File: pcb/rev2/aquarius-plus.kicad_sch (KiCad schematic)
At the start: 216 parts, among them J1 Cassette in, J10 Audio out, J11 Hand controller 2, J12 ESP USB Host, J13 Power in, J14 FPGA spare, J15 Expansion port, J16 ESP32 spare, J2 Cassette out, J3 Amphenol GSD090012SEU, J4 Printer, J5 Hand controller 1, J6 VGA, J7 DBG, J8 USB_A, J9 USB_A, Q1 BC847C, Q2 BC847C, SW1 SW_DPDT_x2, U1 XC3S200-4TQG144, U10 IS61C5128AS-25QLI, U11 74LVC4245APW, U12 74HC166, U13 SST39SF020A-55-4C-WHE, U14 74LVC4245APW, U15 LDL1117S33R, U16 MCP1700T-2502E/TT, U17 LD1117S12, U2 SN74CBTD3861PWR, U3 MAX3221ECPWR, U4 SN74CBTD3861PWR, U5 ESP32-S2-SOLO-N4R2, U6 SN74CBTD3861PWR, U7 Z84C0010AEG, U8 SN74CBTD3861PWR, U9 74HC166, X1 ECS-5032MV-143-CN-TR, X2 ECS-5032MV-480-BN-TR

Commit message: Working on rev2 PCB.
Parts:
- removed C47, C53: 100uF, Capacitor_SMD:CP_Elec_6.3x7.7, symbol Device:C_Polarized_Small
- removed C52, C56, C57, C58, C59, C60: 100nF, Capacitor_SMD:C_0603_1608Metric, symbol Device:C_Small
- removed C63, C66: 4.7uF, Capacitor_SMD:C_0603_1608Metric, symbol Device:C_Small
- removed J8, J9: USB_A, Connector_USB:USB_A_Molex_67643_Horizontal, symbol Connector:USB_A
- removed R10: DNP, Resistor_SMD:R_0603_1608Metric, symbol Device:R
- removed R100: 1, Resistor_SMD:R_0603_1608Metric, symbol Device:R
- removed R11, R2, R5, R6, R63, R64, R65, R66, R67, R68, R69, R70, R8, R91, R92, R93, R94, R95, R96, R97, R98: 4.7k, Resistor_SMD:R_0603_1608Metric, symbol Device:R
- removed R3, R4, R9: 220, Resistor_SMD:R_0603_1608Metric, symbol Device:R
- removed R7: 1k, Resistor_SMD:R_0603_1608Metric, symbol Device:R
- removed R73, R74, R75, R76: 33, Resistor_SMD:R_0603_1608Metric, symbol Device:R
- removed R77, R78, R79, R80: 15k, Resistor_SMD:R_0603_1608Metric, symbol Device:R
- removed U1: XC3S200-4TQG144, Package_QFP:TQFP-144_20x20mm_P0.5mm, symbol aquarius-plus:XC3S200-4TQG144
- removed U11, U14: 74LVC4245APW, Package_SO:TSSOP-24_4.4x7.8mm_P0.65mm, symbol Logic_LevelTranslator:SN74AVC8T245PW
- removed U12, U9: 74HC166, Package_SO:SOIC-16_3.9x9.9mm_P1.27mm, symbol 74xx:74LS166
- removed U13: SST39SF020A-55-4C-WHE, Package_SO:TSOP-I-32_12.4x8mm_P0.5mm, symbol aquarius-plus:SST39SF020A-55-4C-WHE
- removed U16: MCP1700T-2502E/TT, Package_TO_SOT_SMD:SOT-23, symbol Regulator_Linear:MCP1700-2502E_SOT23
- removed U2, U4, U6, U8: SN74CBTD3861PWR, Package_SO:TSSOP-24_4.4x7.8mm_P0.65mm, symbol 74xx:74CBTLV3861
- removed U5: ESP32-S2-SOLO-N4R2, aquarius-plus:ESP32-S2-SOLO-N4R2, symbol aquarius-plus:ESP32-S2-SOLO-N4R2
- removed X2: ECS-5032MV-480-BN-TR, Oscillator:Oscillator_SMD_SeikoEpson_SG8002LB-4Pin_5.0x3.2mm, symbol Oscillator:SG-5032CAN
- added C47: 100nF, Capacitor_SMD:C_0603_1608Metric, symbol Device:C_Small
- added Q3: 2N7002, Package_TO_SOT_SMD:SOT-23, symbol Transistor_FET:2N7002
- added R53: 220, Resistor_SMD:R_0603_1608Metric, symbol Device:R
- added U1: XC6SLX9-2TQG144C, Package_QFP:TQFP-144_20x20mm_P0.5mm, symbol aquarius-plus:XC6SLX9-2TQG144C
- added U11, U2, U4, U6: SN74CB3T3245PWR, Package_SO:TSSOP-20_4.4x6.5mm_P0.65mm, symbol aquarius-plus:SN74CB3T3245PWR
- added U5: ESP32-S3-WROOM-1-N4R2, aquarius-plus:ESP32-S2-SOLO-N4R2, symbol aquarius-plus:ESP32-S3-WROOM-1-N4R2
- added U8, U9: SN74AHCT1G125DBVR, Package_TO_SOT_SMD:SOT-23-5, symbol 74xGxx:74AHCT1G125
- J3: value Amphenol GSD090012SEU -> TF-03A; footprint Connector_Card:SD_TE_2041021 -> aquarius-plus:TF-03A
- R1: value 4.7k -> 10k
- X1: value ECS-5032MV-143-CN-TR -> SX3M14.31818M20F30TNN; footprint Oscillator:Oscillator_SMD_SeikoEpson_SG8002LB-4Pin_5.0x3.2mm -> Oscillator:Oscillator_SMD_SeikoEpson_SG8002CE-4Pin_3.2x2.5mm
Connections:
- net +2V5 is gone; now on net +3V3: C12.1, C17.1, C2.1, C22.1, C26.1, C7.1, R1.2
- net DE0 is gone; now on net D0: J15.26 (Pin_26)
- net DE1 is gone; now on net D1: J15.27 (Pin_27)
- net DE2 is gone; now on net D2: J15.28 (Pin_28)
- net DE3 is gone; now on net D3: J15.29 (Pin_29)
- net DE4 is gone; now on net D4: J15.30 (Pin_30)
- net DE5 is gone; now on net D5: J15.31 (Pin_31)
- net DE6 is gone; now on net D6: J15.32 (Pin_32)
- net DE7 is gone; now on net D7: J15.33 (Pin_33)
- net +1V2: now also C30.1, U1.128 (VCCINT), U1.19 (VCCINT), U1.28 (VCCINT), U1.52 (VCCINT), U1.89 (VCCINT)
- net +3V3: now also C35.1, C42.1, C43.1, C47.1, U1.103 (VCCO_1), U1.122 (VCCO_0), U1.125 (VCCO_0), U1.129 (VCCAUX), U1.135 (VCCO_0), U1.18 (VCCO_3), U1.20 (VCCAUX), U1.31 (VCCO_3), U1.36 (VCCAUX), U1.4 (VCCO_3), U1.42 (VCCO_2), U1.53 (VCCAUX), U1.60 (B2_IO_M1), U1.63 (VCCO_2), U1.69 (B2_IO_M0), U1.76 (VCCO_1), U1.86 (VCCO_1), U1.90 (VCCAUX), U11.20 (VCC), U2.20 (VCC), U4.20 (VCC), U5.2 (3V3), U6.20 (VCC); no longer C30.1, C51.1
- net +5V: now also C51.1, U8.5 (VCC), U9.5 (VCC); no longer C35.1, C42.1, C43.1
- net A0: now also U11.18 (B1)
- net A1: now also U11.17 (B2)
- net A10: now also U2.16 (B3)
- net A11: now also U2.15 (B4)
- net A12: now also U2.14 (B5)
- net A13: now also U2.13 (B6)
- net A14: now also U2.12 (B7)
- net A15: now also U2.11 (B8)
- net A2: now also U11.16 (B3)
- net A3: now also U11.15 (B4)
- net A4: now also U11.14 (B5)
- net A5: now also U11.13 (B6)
- net A6: now also U11.12 (B7)
- net A7: now also U11.11 (B8)
- net A8: now also U2.18 (B1)
- net A9: now also U2.17 (B2)
- net AUDIO_L: now also U1.22 (B3_IO_GCLK25)
- net AUDIO_R: now also U1.21 (B3_IO_GCLK24)
- net BA14: now also U1.143 (B0_IO_VREF)
- net BA15: now also U1.142 (B0_IO)
- net BA16: now also U1.141 (B0_IO)
- net BA17: now also U1.140 (B0_IO)
- net BA18: now also U1.139 (B0_IO)
- net BUSACK#: now also U6.11 (B8)
- net BUSREQ#: now also U6.12 (B7)
- net CART_CE#: now also U9.4
- net CASSETTE_IN: now also U1.24 (B3_IO_GCLK27)
- net CASSETTE_OUT: now also U1.23 (B3_IO_GCLK26)
- net D0: now also U4.18 (B1)
- net D1: now also U4.17 (B2)
- net D2: now also U4.16 (B3)
- net D3: now also U4.15 (B4)
- net D4: now also U4.14 (B5)
- net D5: now also U4.13 (B6)
- net D6: now also U4.12 (B7)
- net D7: now also U4.11 (B8)
- net ESP_CTS: now also U1.29 (B3_IO), U5.24 (IO47)
- net ESP_EXP0: now also U5.39 (IO1)
- net ESP_EXP1: now also U5.38 (IO2)
- net ESP_EXP2: now also U5.35 (IO42)
- net ESP_EXP3: now also U5.34 (IO41)
- net ESP_EXP4: now also U5.33 (IO40)
- net ESP_EXP5: now also U5.32 (IO39)
- net ESP_EXP6: now also U5.31 (IO38)
- net ESP_EXP7: now also U5.30 (IO37)
- net ESP_NOTIFY: now also U1.34 (B3_IO_VREF), U5.20 (IO12)
- net ESP_RTS: now also U1.32 (B3_IO), U5.22 (IO14)
- net ESP_RX: now also U1.30 (B3_IO), U5.23 (IO21)
- net ESP_TX: now also U1.33 (B3_IO), U5.21 (IO13)
- net ESP_USB_DM: now also U5.13 (IO19/USB_DM)
- net ESP_USB_DP: now also U5.14 (IO20/USB_DP)
- net FPGA_A0: now also U1.138 (B0_IO), U11.2 (A1)
- net FPGA_A1: now also U1.137 (B0_IO), U11.3 (A2)
- net FPGA_A10: now also U1.121 (B0_IO), U2.4 (A3)
- net FPGA_A11: now also U1.120 (B0_IO_VREF), U2.5 (A4)
- net FPGA_A12: now also U1.119 (B0_IO), U2.6 (A5)
- net FPGA_A13: now also U1.118 (B0_IO), U2.7 (A6)
- net FPGA_A14: now also U1.117 (B0_IO), U2.8 (A7)
- net FPGA_A15: now also U1.116 (B0_IO), U2.9 (A8)
- net FPGA_A2: now also U1.134 (B0_IO_GCLK19), U11.4 (A3)
- net FPGA_A3: now also U1.133 (B0_IO_GCLK18), U11.5 (A4)
- net FPGA_A4: now also U1.132 (B0_IO_GCLK17), U11.6 (A5)
- net FPGA_A5: now also U1.131 (B0_IO_GCLK16), U11.7 (A6)
- net FPGA_A6: now also U1.127 (B0_IO_GCLK15), U11.8 (A7)
- net FPGA_A7: now also U1.126 (B0_IO_GCLK14), U11.9 (A8)
- net FPGA_A8: now also U1.124 (B0_IO_GCLK13), U2.2 (A1)
- net FPGA_A9: now also U1.123 (B0_IO_GCLK12), U2.3 (A2)
- net FPGA_BUSACK#: now also U1.92 (B1_IO_GCLK8), U6.9 (A8)
- net FPGA_BUSREQ#: now also U1.93 (B1_IO_GCLK9), U6.8 (A7)
- net FPGA_CART_CE#: now also U1.88 (B1_IO_GCLK7), U9.2
- net FPGA_D0: now also U1.115 (B0_IO), U4.2 (A1)
- net FPGA_D1: now also U1.114 (B0_IO), U4.3 (A2)
- net FPGA_D2: now also U1.112 (B0_IO), U4.4 (A3)
- net FPGA_D3: now also U1.111 (B0_IO), U4.5 (A4)
- net FPGA_D4: now also U1.105 (B1_IO), U4.6 (A5)
- net FPGA_D5: now also U1.104 (B1_IO_VREF), U4.7 (A6)
- net FPGA_D6: now also U1.102 (B1_IO), U4.8 (A7)
- net FPGA_D7: now also U1.101 (B1_IO), U4.9 (A8)
- net FPGA_DONE: now also U1.71 (DONE), U5.12 (IO8)
- net FPGA_INT#: now also U1.95 (B1_IO_GCLK11), U6.6 (A5)
- net FPGA_IORQ#: now also U1.99 (B1_IO), U6.3 (A2)
- net FPGA_MREQ#: now also U1.100 (B1_IO), U6.2 (A1)
- net FPGA_PHI: now also U1.87 (B1_IO_GCLK6), U8.2
- net FPGA_PROG#: now also U1.37 (PROG_B), U5.25 (IO48)
- net FPGA_RD#: now also U1.98 (B1_IO), U6.4 (A3)
- net FPGA_RESET#: now also U1.94 (B1_IO_GCLK10), U6.7 (A6)
- net FPGA_WR#: now also U1.97 (B1_IO), U6.5 (A4)
- net GND: now also C47.2, Q3.2 (S), U1.108 (GND), U1.113 (GND), U1.13 (GND), U1.130 (GND), U1.136 (GND), U1.25 (GND), U1.3 (GND), U1.49 (GND), U1.54 (GND), U1.68 (GND), U1.73 (SUSPEND), U1.77 (GND), U1.91 (GND), U1.96 (GND), U11.10 (GND), U11.19 (~{OE}), U2.10 (GND), U2.19 (~{OE}), U4.10 (GND), U4.19 (~{OE}), U5.1 (GND), U5.40 (GND), U5.41 (EPAD), U6.10 (GND), U6.19 (~{OE}), U8.1, U8.3 (GND), U9.1, U9.3 (GND)
- net INT#: now also U6.14 (B5)
- net IORQ#: now also U6.17 (B2)
- net MREQ#: now also U6.18 (B1)
- net PHI: now also U8.4
- net PRINTER_IN: now also U1.26 (B3_IO)
- net PRINTER_OUT: now also U1.27 (B3_IO)
- net RAM_CE#: now also U1.85 (B1_IO_GCLK5)
- net RD#: now also U6.16 (B3)
- net RESET#: now also U6.13 (B6)
- net SD_ACTIVITY: now also U5.4 (IO4)
- net SD_MISO: now also U5.7 (IO7)
- net SD_MOSI: now also U5.9 (IO16)
- net SD_SCK: now also U5.8 (IO15)
- net SD_SSEL#: now also U5.10 (IO17)
- net SD_WP#: now also Q3.3 (D), U5.5 (IO5); no longer J3.11 (WRITE_PROTECT)
- net SPI_CS#: now also U1.74 (B2_IO_DOUT), U5.19 (IO11)
- net SPI_MISO: now also U1.39 (B2_IO_INIT_B), U5.15 (IO3)
- net SPI_MOSI: now also U1.65 (B2_IO_DIN), U5.17 (IO9)
- net SPI_SCLK: now also R53.1, U5.18 (IO10)
- net SYSCLK: now also U1.84 (B1_IO_GCLK4)
- net VGA_B0: now also U1.5 (B3_IO)
- net VGA_B1: now also U1.6 (B3_IO)
- net VGA_B2: now also U1.7 (B3_IO)
- net VGA_B3: now also U1.8 (B3_IO)
- net VGA_G0: now also U1.9 (B3_IO)
- net VGA_G1: now also U1.10 (B3_IO)
- net VGA_G2: now also U1.11 (B3_IO)
- net VGA_G3: now also U1.12 (B3_IO)
- net VGA_HSYNC: now also U1.1 (B3_IO)
- net VGA_R0: now also U1.14 (B3_IO_GCLK20)
- net VGA_R1: now also U1.15 (B3_IO_GCLK21)
- net VGA_R2: now also U1.16 (B3_IO_GCLK22)
- net VGA_R3: now also U1.17 (B3_IO_GCLK23)
- net VGA_VSYNC: now also U1.2 (B3_IO)
- net WR#: now also U6.15 (B4)
- net HC2_D02: now reaches R86.2
- net HC2_D06: now reaches R87.2
- net at R1.1: now also J3.11 (WRITE_PROTECT), Q3.1 (G)
- net HC1_D07: now reaches R61.2
- net at JP1.1 (A): now also U5.27 (IO0)
- net at C36.1, R27.2: now also U5.3 (EN)
- net at J7.2 (Pin_2): now also U5.36 (IO44/RXD0)
- net at J7.1 (Pin_1): now also U5.37 (IO43/TXD0)
- net HC1_D03: now reaches R56.2
- net HC1_D05: now reaches R57.2
- net HC1_D01: now reaches R60.2
- net HC2_D05: now reaches R85.2
- net HC1_D04: now reaches R55.2
- net HC1_D00: now reaches R62.2
- net HC1_D06: now reaches R59.2
- net HC2_D01: now reaches R88.2
- net HC2_D00: now reaches R90.2
- net HC2_D04: now reaches R83.2
- net HC2_D03: now reaches R84.2
- net HC1_D02: now reaches R58.2
- net HC2_D07: now reaches R89.2
- net RAM_ROM_WE# renamed RAM_WE#
- net RAM_WE#: now also U1.83 (B1_IO)
- net SD_CD# renamed SD_CD
- net SD_CD: now also U5.6 (IO6)
- new net: R53.2, U1.70 (B2_IO_CCLK)
- no-connect marks 21 -> 20
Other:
- note removed: "256KB Flash"
- note removed: "USB clock (48MHz)"
- note removed: "USB host via FPGA"
- moved on the sheet: C1, C10, C11, C12, C13, C14, C15, C16, C17, C18, C19, C2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

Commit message: A little work on rev2
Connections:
- net BA14: now also U1.79 (B1_IO); no longer U1.143 (B0_IO_VREF)
- net BA15: now also U1.80 (B1_IO); no longer U1.142 (B0_IO)
- net BA16: now also U1.78 (B1_IO); no longer U1.141 (B0_IO)
- net BA17: now also U1.75 (B1_IO_AWAKE); no longer U1.140 (B0_IO)
- net BA18: now also U1.81 (B1_IO); no longer U1.139 (B0_IO)
- net FPGA_A0: now also U1.134 (B0_IO_GCLK19); no longer U1.138 (B0_IO)
- net FPGA_A1: now also U1.133 (B0_IO_GCLK18); no longer U1.137 (B0_IO)
- net FPGA_A10: now also U1.119 (B0_IO); no longer U1.121 (B0_IO)
- net FPGA_A11: now also U1.118 (B0_IO); no longer U1.120 (B0_IO_VREF)
- net FPGA_A12: now also U1.117 (B0_IO); no longer U1.119 (B0_IO)
- net FPGA_A13: now also U1.116 (B0_IO); no longer U1.118 (B0_IO)
- net FPGA_A14: now also U1.115 (B0_IO); no longer U1.117 (B0_IO)
- net FPGA_A15: now also U1.114 (B0_IO); no longer U1.116 (B0_IO)
- net FPGA_A2: now also U1.132 (B0_IO_GCLK17); no longer U1.134 (B0_IO_GCLK19)
- net FPGA_A3: now also U1.131 (B0_IO_GCLK16); no longer U1.133 (B0_IO_GCLK18)
- net FPGA_A4: now also U1.127 (B0_IO_GCLK15); no longer U1.132 (B0_IO_GCLK17)
- net FPGA_A5: now also U1.126 (B0_IO_GCLK14); no longer U1.131 (B0_IO_GCLK16)
- net FPGA_A6: now also U1.124 (B0_IO_GCLK13); no longer U1.127 (B0_IO_GCLK15)
- net FPGA_A7: now also U1.123 (B0_IO_GCLK12); no longer U1.126 (B0_IO_GCLK14)
- net FPGA_A8: now also U1.121 (B0_IO); no longer U1.124 (B0_IO_GCLK13)
- net FPGA_A9: now also U1.120 (B0_IO_VREF); no longer U1.123 (B0_IO_GCLK12)
- net FPGA_BUSACK#: now also U1.87 (B1_IO_GCLK6); no longer U1.92 (B1_IO_GCLK8)
- net FPGA_BUSREQ#: now also U1.88 (B1_IO_GCLK7); no longer U1.93 (B1_IO_GCLK9)
- net FPGA_CART_CE#: now also U1.85 (B1_IO_GCLK5); no longer U1.88 (B1_IO_GCLK7)
- net FPGA_D0: now also U1.112 (B0_IO); no longer U1.115 (B0_IO)
- net FPGA_D1: now also U1.111 (B0_IO); no longer U1.114 (B0_IO)
- net FPGA_D2: now also U1.105 (B1_IO); no longer U1.112 (B0_IO)
- net FPGA_D3: now also U1.104 (B1_IO_VREF); no longer U1.111 (B0_IO)
- net FPGA_D4: now also U1.102 (B1_IO); no longer U1.105 (B1_IO)
- net FPGA_D5: now also U1.101 (B1_IO); no longer U1.104 (B1_IO_VREF)
- net FPGA_D6: now also U1.100 (B1_IO); no longer U1.102 (B1_IO)
- net FPGA_D7: now also U1.99 (B1_IO); no longer U1.101 (B1_IO)
- net FPGA_INT#: now also U1.93 (B1_IO_GCLK9); no longer U1.95 (B1_IO_GCLK11)
- net FPGA_IORQ#: now also U1.97 (B1_IO); no longer U1.99 (B1_IO)
- net FPGA_MREQ#: now also U1.98 (B1_IO); no longer U1.100 (B1_IO)
- net FPGA_PHI: now also U1.84 (B1_IO_GCLK4); no longer U1.87 (B1_IO_GCLK6)
- net FPGA_RD#: now also U1.95 (B1_IO_GCLK11); no longer U1.98 (B1_IO)
- net FPGA_RESET#: now also U1.92 (B1_IO_GCLK8); no longer U1.94 (B1_IO_GCLK10)
- net FPGA_WR#: now also U1.94 (B1_IO_GCLK10); no longer U1.97 (B1_IO)
- net RAM_CE#: now also U1.83 (B1_IO); no longer U1.85 (B1_IO_GCLK5)
- net RAM_WE#: now also U1.82 (B1_IO); no longer U1.83 (B1_IO)
- net SYSCLK: now also U1.55 (B2_IO_GCLK0); no longer U1.84 (B1_IO_GCLK4)

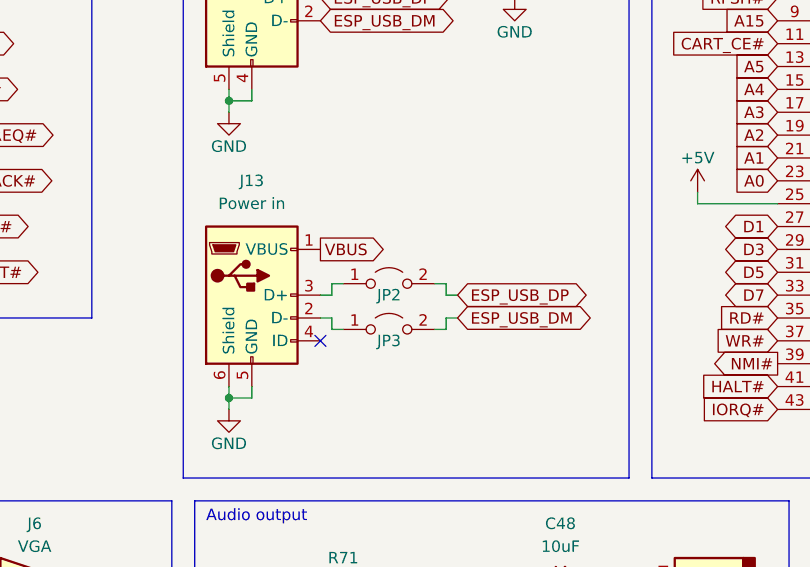
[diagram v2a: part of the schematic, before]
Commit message: Continued wiring rev2
Replaced the 2-lug USB micro power with a similar 4-lug model in the same family, orderable through JLCPCB.
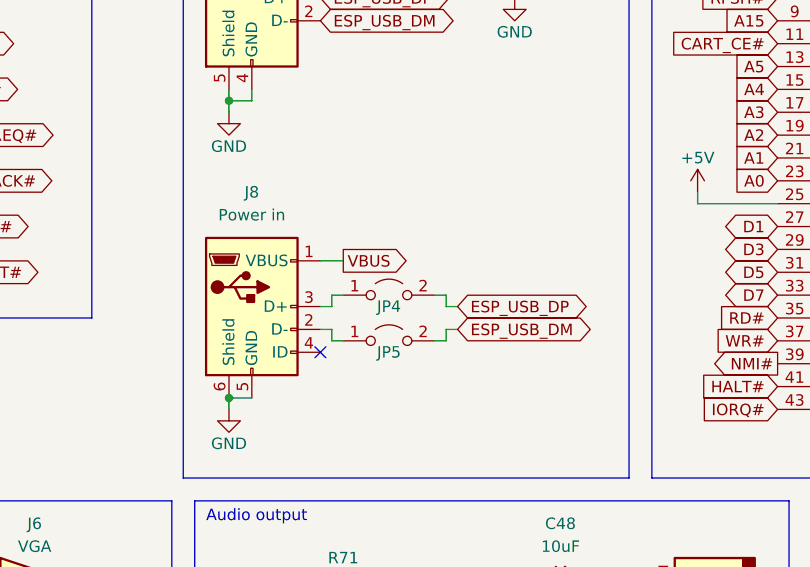
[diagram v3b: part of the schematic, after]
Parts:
- removed J13: Power in, aquarius-plus:10118193-0001LF, symbol Connector:USB_B_Micro
- removed JP2, JP3: USB, Connector_PinHeader_2.54mm:PinHeader_1x02_P2.54mm_Vertical, symbol Jumper:Jumper_2_Open
- added J8: Power in, aquarius-plus:AMPHENOL_10118194-0001LF, symbol Connector:USB_B_Micro
- added JP4, JP5: USB, Connector_PinHeader_2.54mm:PinHeader_1x02_P2.54mm_Vertical, symbol Jumper:Jumper_2_Open
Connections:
- net ESP_USB_DM: now also JP5.2 (B)
- net ESP_USB_DP: now also JP4.2 (B)
- net GND: now also J8.5 (GND), J8.6 (Shield)
- net VBUS: now also J8.1 (VBUS)
- new net: J8.2 (D-), JP5.1 (A)
- new net: J8.3 (D+), JP4.1 (A)

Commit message: rev2 updates
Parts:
- added R2, R3: 100, Resistor_SMD:R_0603_1608Metric, symbol Device:R
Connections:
- net GND: no longer J11.1, J5.1
- new net: J5.1, R2.1
- new net: J11.1, R3.1
- new net HC1_D08: R2.2
- new net HC2_D08: R3.2
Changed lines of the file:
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@@
     (stroke (width 0) (type solid))
   )
-  (wire (pts (xy 224.79 304.8) (xy 224.79 306.07))
-    (stroke (width 0) (type default))
-  )
   (wire (pts (xy 176.53 22.86) (xy 176.53 26.67))
     (stroke (width 0) (type default))
@@
     (stroke (width 0) (type default))
   )
-  (wire (pts (xy 223.52 304.8) (xy 224.79 304.8))
-    (stroke (width 0) (type default))
-  )
   (wire (pts (xy 191.77 100.33) (xy 185.42 100.33))
     (stroke (width 0) (type default))
@@
     (stroke (width 0) (type default))
   )
-  (wire (pts (xy 266.7 304.8) (xy 267.97 304.8))
-    (stroke (width 0) (type default))
-  )
   (wire (pts (xy 196.85 100.33) (xy 191.77 100.33))
     (stroke (width 0) (type default))
@@
     (stroke (width 0) (type solid))
   )
-  (wire (pts (xy 267.97 304.8) (xy 267.97 306.07))
-    (stroke (width 0) (type default))
-  )
   (polyline (pts (xy 237.49 13.97) (xy 237.49 81.28))
     (stroke (width 0) (type solid))
@@
     (stroke (width 0) (type default))
   )
+  (wire (pts (xy 274.32 304.8) (xy 279.4 304.8))
+    (stroke (width 0) (type default))
+  )
   (wire (pts (xy 254 81.28) (xy 255.27 81.28))
     (stroke (width 0) (type default))
@@
     (stroke (width 0) (type solid))
   )
+  (wire (pts (xy 231.14 304.8) (xy 236.22 304.8))
+    (stroke (width 0) (type default))
+  )
   (wire (pts (xy 233.68 255.27) (xy 234.95 255.27))
     (stroke (width 0) (type default))
@@
     )
   )
+  (global_label "HC2_D08" (shape bidirectional) (at 279.4 304.8 0) (fields_autoplaced)
+    (effects (font (size 1.27 1.27)) (justify left))
+    (property "Intersheetrefs" "${INTERSHEET_REFS}" (at 291.8837 304.8 0)
+      (effects (font (size 1.27 1.27)) (justify left) hide)
+    )
+  )
   (global_label "SPI_SCLK" (shape output) (at 177.8 69.85 180) (fields_autoplaced)
     (effects (font (size 1.27 1.27)) (justify right))
@@
     )
   )
+  (global_label "HC1_D08" (shape bidirectional) (at 236.22 304.8 0) (fields_autoplaced)
+    (effects (font (size 1.27 1.27)) (justify left))
+    (property "Intersheetrefs" "${INTERSHEET_REFS}" (at 248.7037 304.8 0)
+      (effects (font (size 1.27 1.27)) (justify left) hide)
+    )
+  )
   (global_label "SD_SSEL#" (shape output) (at 177.8 49.53 180) (fields_autoplaced)
     (effects (font (size 1.27 1.27)) (justify right))
@@
     )
   )
-  (symbol (lib_id "power:GND") (at 224.79 306.07 0) (mirror y) (unit 1)
-    (in_bom yes) (on_board yes) (dnp no)
-    (property "Reference" "#PWR078" (at 224.79 312.42 0)
-      (effects (font (size 1.27 1.27)) hide)
-    )
-    (property "Value" "GND" (at 224.79 309.88 0)
-      (effects (font (size 1.27 1.27)))
-    )
-    (property "Footprint" "" (at 224.79 306.07 0)
-      (effects (font (size 1.27 1.27)) hide)
-    )
-    (property "Datasheet" "" (at 224.79 306.07 0)
-      (effects (font (size 1.27 1.27)) hide)
-    )
-    (pin "1")
-    (instances
-      (project "aquarius-plus"
-        (path "/e63e39d7-6ac0-4ffd-8aa3-1841a4541b55"
-          (reference "#PWR078") (unit 1)
-        )
-      )
-    )
-  )
   (symbol (lib_id "Device:C_Small") (at 401.32 49.53 0) (unit 1)
     (in_bom yes) (on_board yes) (dnp no) (fields_autoplaced)
@@
     )
   )
-  (symbol (lib_id "power:GND") (at 267.97 306.07 0) (mirror y) (unit 1)
-    (in_bom yes) (on_board yes) (dnp no)
-    (property "Reference" "#PWR0118" (at 267.97 312.42 0)
-      (effects (font (size 1.27 1.27)) hide)
-    )
-    (property "Value" "GND" (at 267.97 309.88 0)
-      (effects (font (size 1.27 1.27)))
-    )
-    (property "Footprint" "" (at 267.97 306.07 0)
-      (effects (font (size 1.27 1.27)) hide)
-    )
-    (property "Datasheet" "" (at 267.97 306.07 0)
-      (effects (font (size 1.27 1.27)) hide)
-    )
-    (pin "1")
-    (instances
-      (project "aquarius-plus"
-        (path "/e63e39d7-6ac0-4ffd-8aa3-1841a4541b55"
-          (reference "#PWR0118") (unit 1)
-        )
-      )
-    )
-  )
   (symbol (lib_id "Device:C_Small") (at 44.45 302.26 0) (unit 1)
     (in_bom yes) (on_board yes) (dnp no) (fields_autoplaced)
@@
     )
   )
+  (symbol (lib_id "Device:R") (at 227.33 304.8 90) (unit 1)
+    (in_bom yes) (on_board yes) (dnp no)
+    (property "Reference" "R2" (at 231.775 303.53 90)
+      (effects (font (size 1.27 1.27)))
+    )
+    (property "Value" "100" (at 227.33 304.8 90)
+      (effects (font (size 1.27 1.27)))
+    )
+    (property "Footprint" "Resistor_SMD:R_0603_1608Metric" (at 227.33 306.578 90)
+      (effects (font (size 1.27 1.27)) hide)
+    )
+    (property "Datasheet" "~" (at 227.33 304.8 0)
+      (effects (font (size 1.27 1.27)) hide)
+    )
+    (pin "1")
+    (pin "2")
+    (instances
+      (project "aquarius-plus"
+        (path "/e63e39d7-6ac0-4ffd-8aa3-1841a4541b55"
+          (reference "R2") (unit 1)
+        )
+      )
+    )
+  )
   (symbol (lib_id "power:GND") (at 163.83 205.74 0) (unit 1)
     (in_bom yes) (on_board yes) (dnp no)
@@
         )
       )
+    )
+  )
+  (symbol (lib_id "Device:R") (at 270.51 304.8 90) (unit 1)
+    (in_bom yes) (on_board yes) (dnp no)
+    (property "Reference" "R3" (at 274.955 303.53 90)
+      (effects (font (size 1.27 1.27)))
+    )
+    (property "Value" "100" (at 270.51 304.8 90)
+      (effects (font (size 1.27 1.27)))
+    )
+    (property "Footprint" "Resistor_SMD:R_0603_1608Metric" (at 270.51 306.578 90)
+      (effects (font (size 1.27 1.27)) hide)
+    )
+    (property "Datasheet" "~" (at 270.51 304.8 0)
+      (effects (font (size 1.27 1.27)) hide)
+    )
+    (pin "1")
+    (pin "2")
+    (instances
+      (project "aquarius-plus"
+        (path "/e63e39d7-6ac0-4ffd-8aa3-1841a4541b55"
+          (reference "R3") (unit 1)
+        )
+      )
